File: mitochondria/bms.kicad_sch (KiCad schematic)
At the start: 14 parts, among them U1 BQ7791504PW

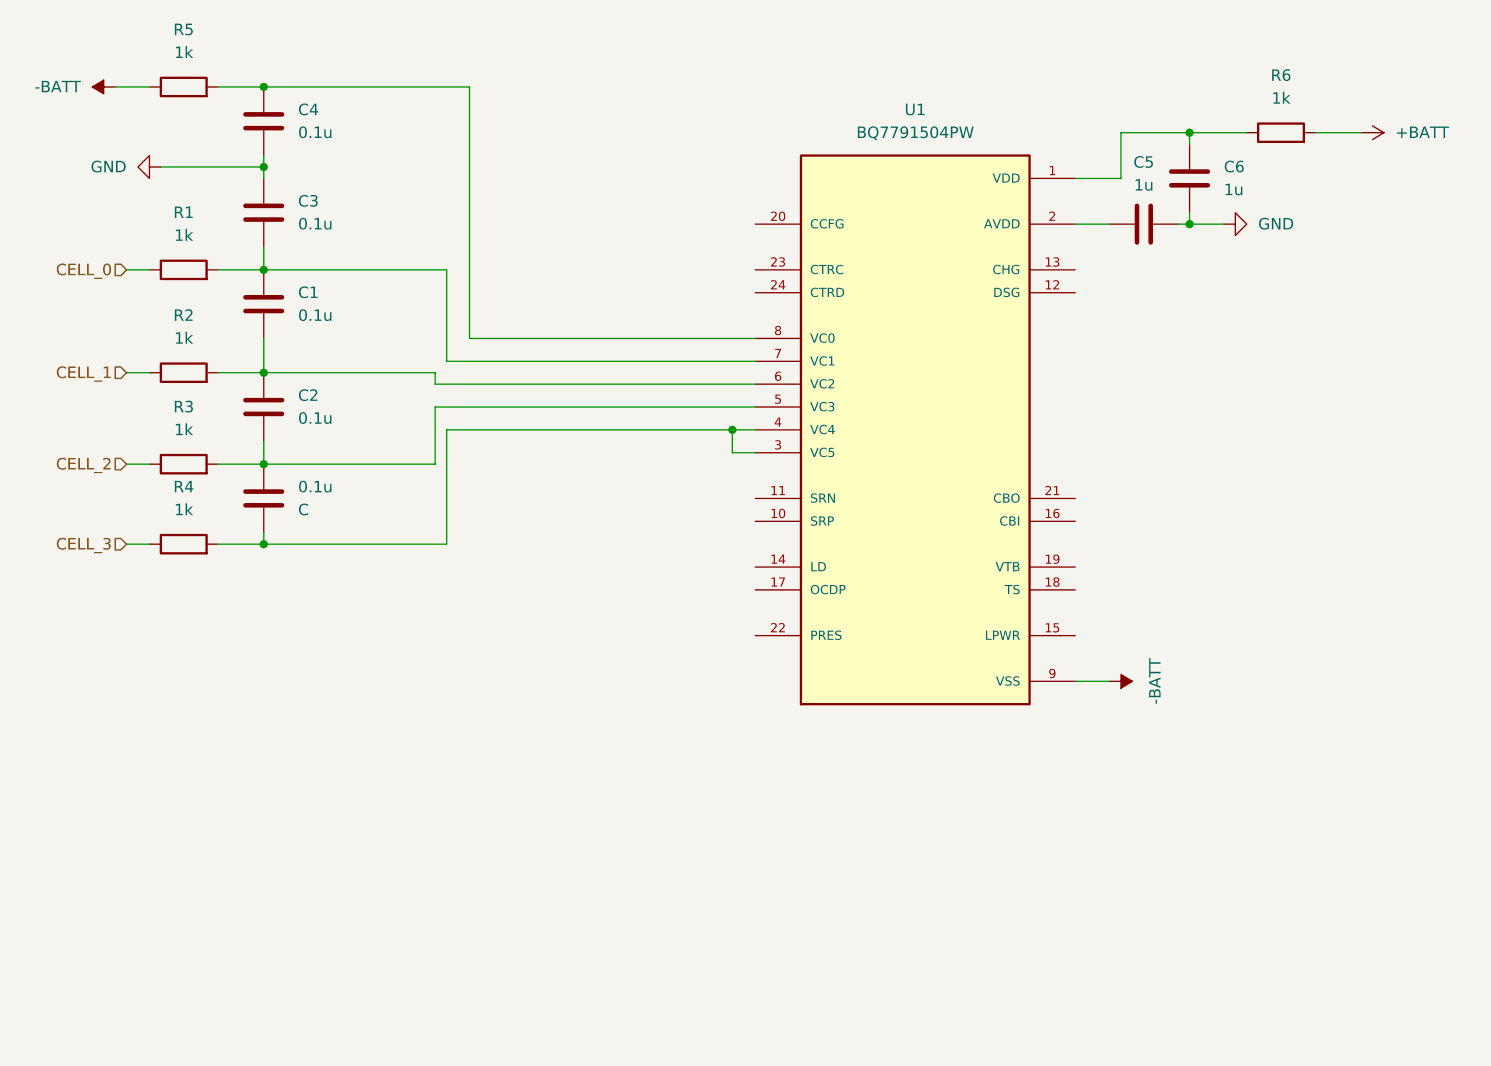
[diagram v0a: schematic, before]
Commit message: alpha 0.1.1: Unified versions, completed BMS + new subschematics
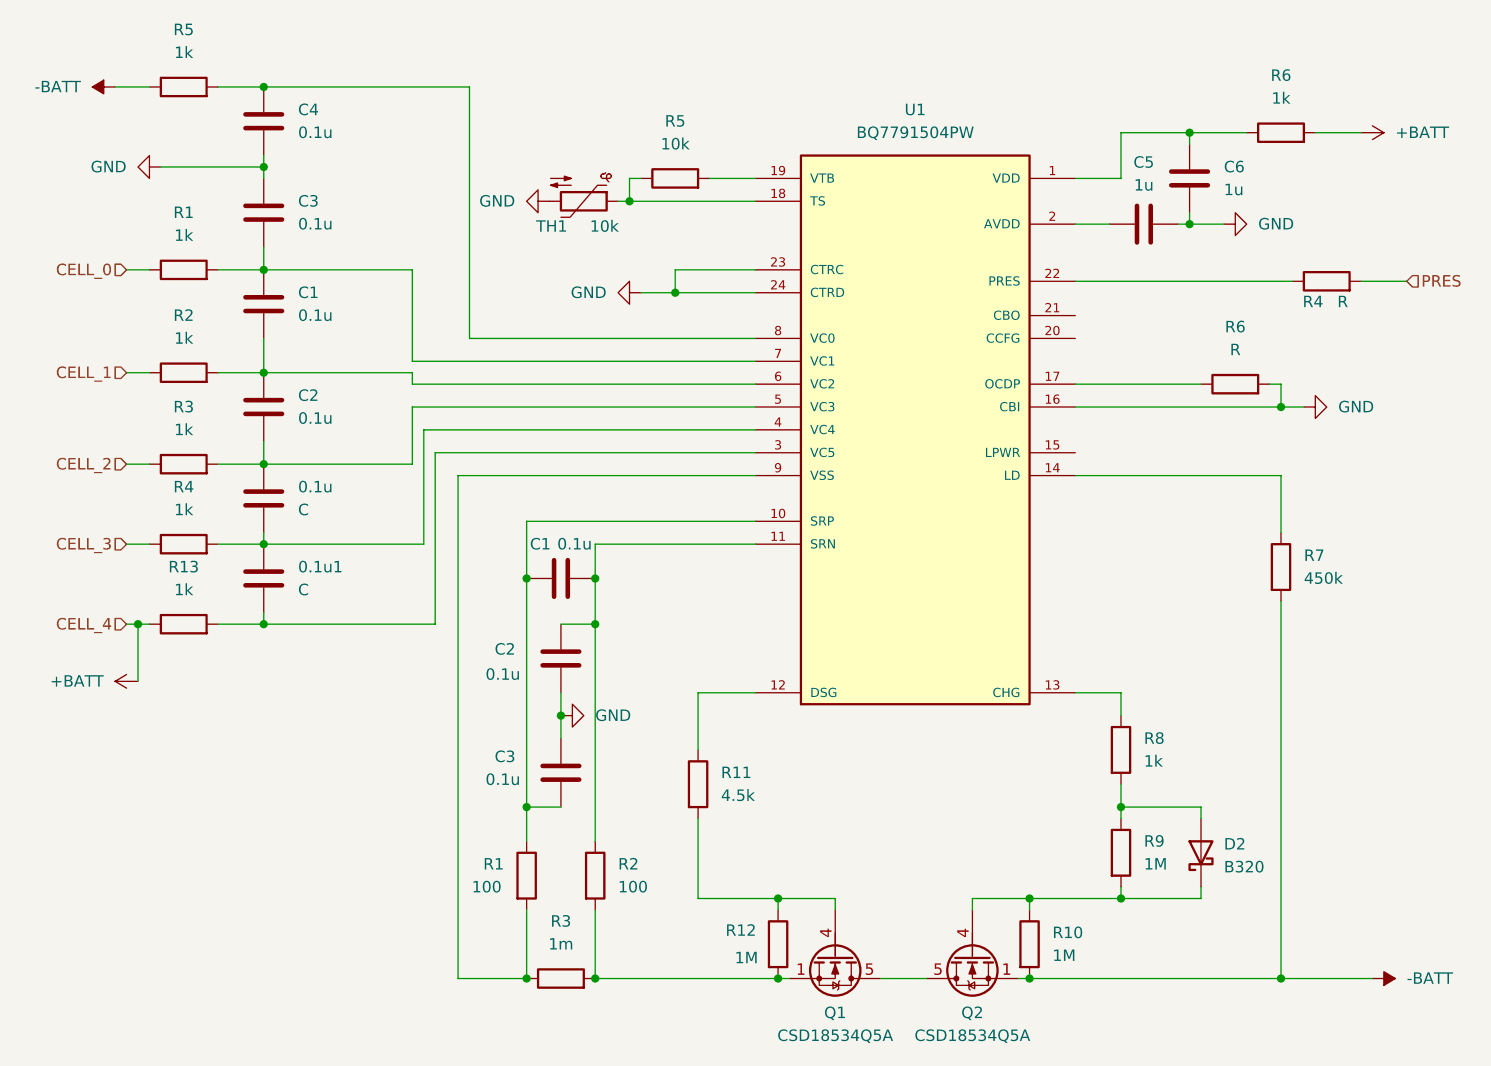
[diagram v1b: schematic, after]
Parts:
- added 0.1u1: C, symbol Device:C
- added C1, C2, C3: 0.1u, symbol Device:C
- added D2: B320, Diode_SMD:D_SMC, symbol Diode:B320
- added Q1, Q2: CSD18534Q5A, Package_TO_SOT_SMD:TDSON-8-1, symbol Transistor_FET:CSD18534Q5A
- added R1, R2: 100, symbol Device:R
- added R10, R12, R9: 1M, symbol Device:R
- added R11: 4.5k, symbol Device:R
- added R13, R8: 1k, symbol Device:R
- added R3: 1m, symbol Device:R
- added R4, R6: R, symbol Device:R
- added R5: 10k, symbol Device:R
- added R7: 450k, symbol Device:R
- added TH1: 10k, symbol Device:Thermistor_NTC
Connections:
- net +BATT: now also R13.1
- net -BATT: now also Q2.1 (S), Q2.2 (S), Q2.3 (S), R10.2, R7.2; no longer U1.9 (VSS)
- net GND: now also U1.16 (CBI), U1.23 (CTRC), U1.24 (CTRD), C2.2, C3.1, R6.2, TH1.2
- net at 0.1u.2, R4.2, U1.4 (VC4): now also 0.1u1.1; no longer U1.3 (VC5)
- net at U1.10 (SRP): now also C1.1, C3.2, R1.1
- net at U1.11 (SRN): now also C1.2, C2.1, R2.1
- net at U1.12 (DSG): now also R11.1
- net at U1.13 (CHG): now also R8.1
- net at U1.14 (LD): now also R7.1
- net at U1.17 (OCDP): now also R6.1
- net at U1.18 (TS): now also R5.1, TH1.1
- net at U1.19 (VTB): now also R5.2
- net at U1.22 (PRES): now also R4.1
- new net: Q1.4 (G), R11.2, R12.1
- new net: 0.1u1.2, R13.2, U1.3 (VC5)
- new net: D2.2 (A), R8.2, R9.1
- new net: D2.1 (K), Q2.4 (G), R10.1, R9.2
- new net: Q1.1 (S), Q1.2 (S), Q1.3 (S), R12.2, R2.2, R3.2
- new net: Q1.5 (D), Q2.5 (D)
- new net: R1.2, R3.1, U1.9 (VSS)
- new net PRES: R4.2
